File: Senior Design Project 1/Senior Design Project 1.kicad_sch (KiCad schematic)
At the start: 30 parts, among them U1 74LS05, U2 74HC273, U3 LM393NG, U6 LM555xN, U9 74HC273

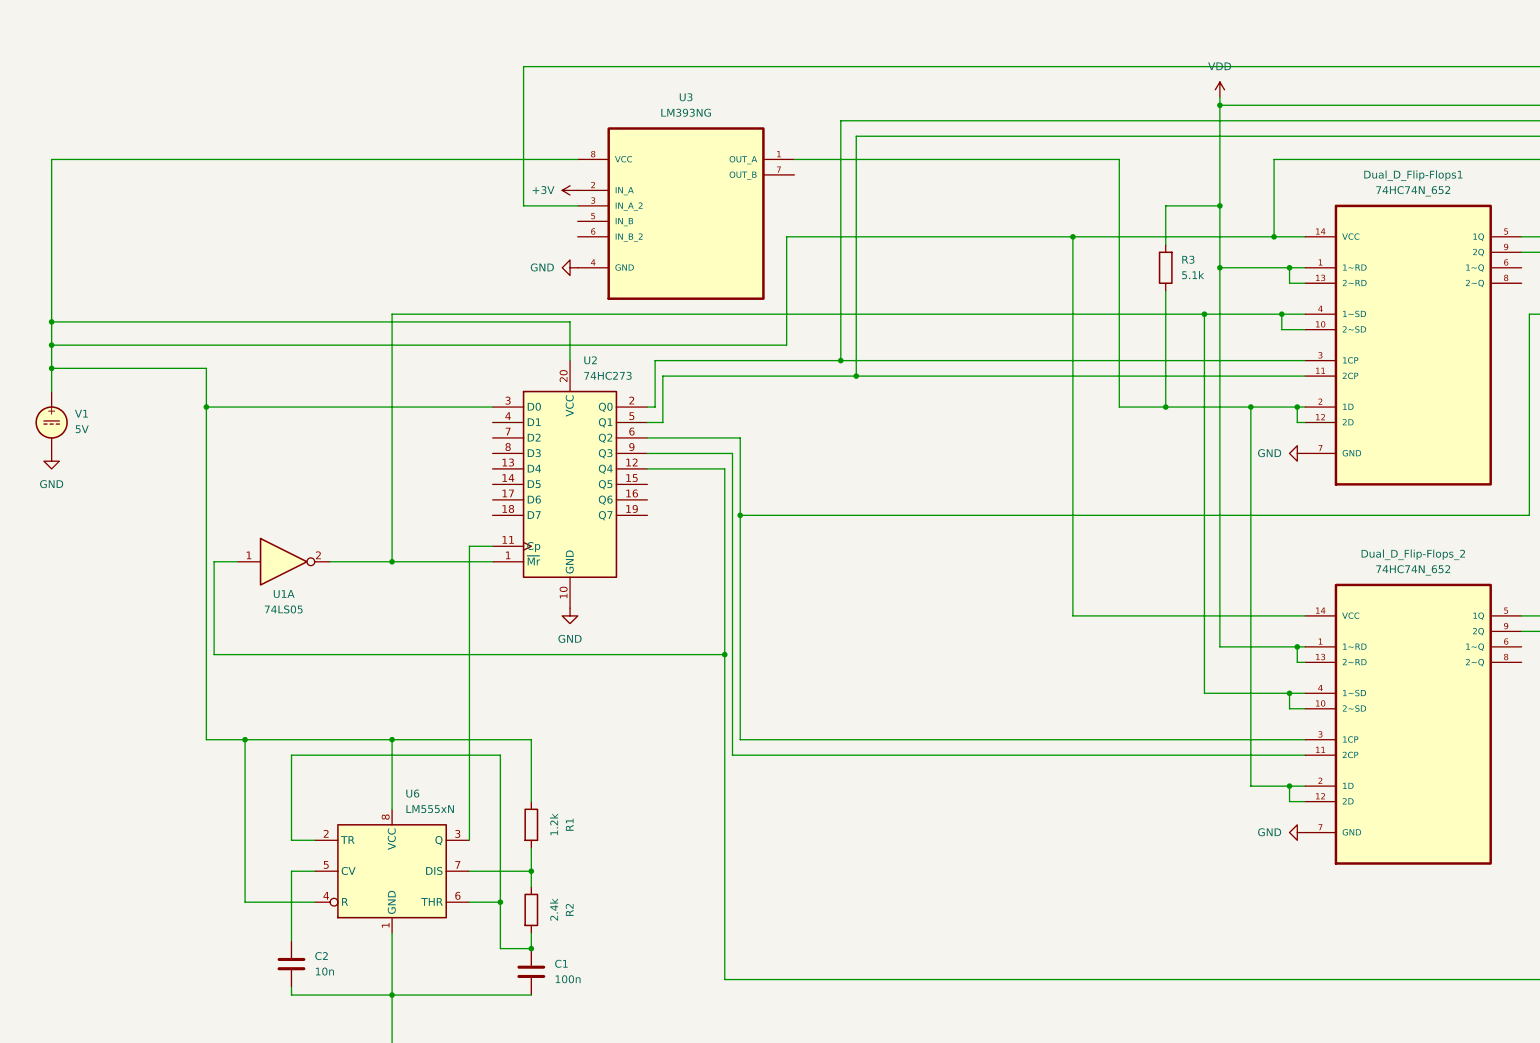
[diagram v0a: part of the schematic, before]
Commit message: Footprint fixes and updated PCB design
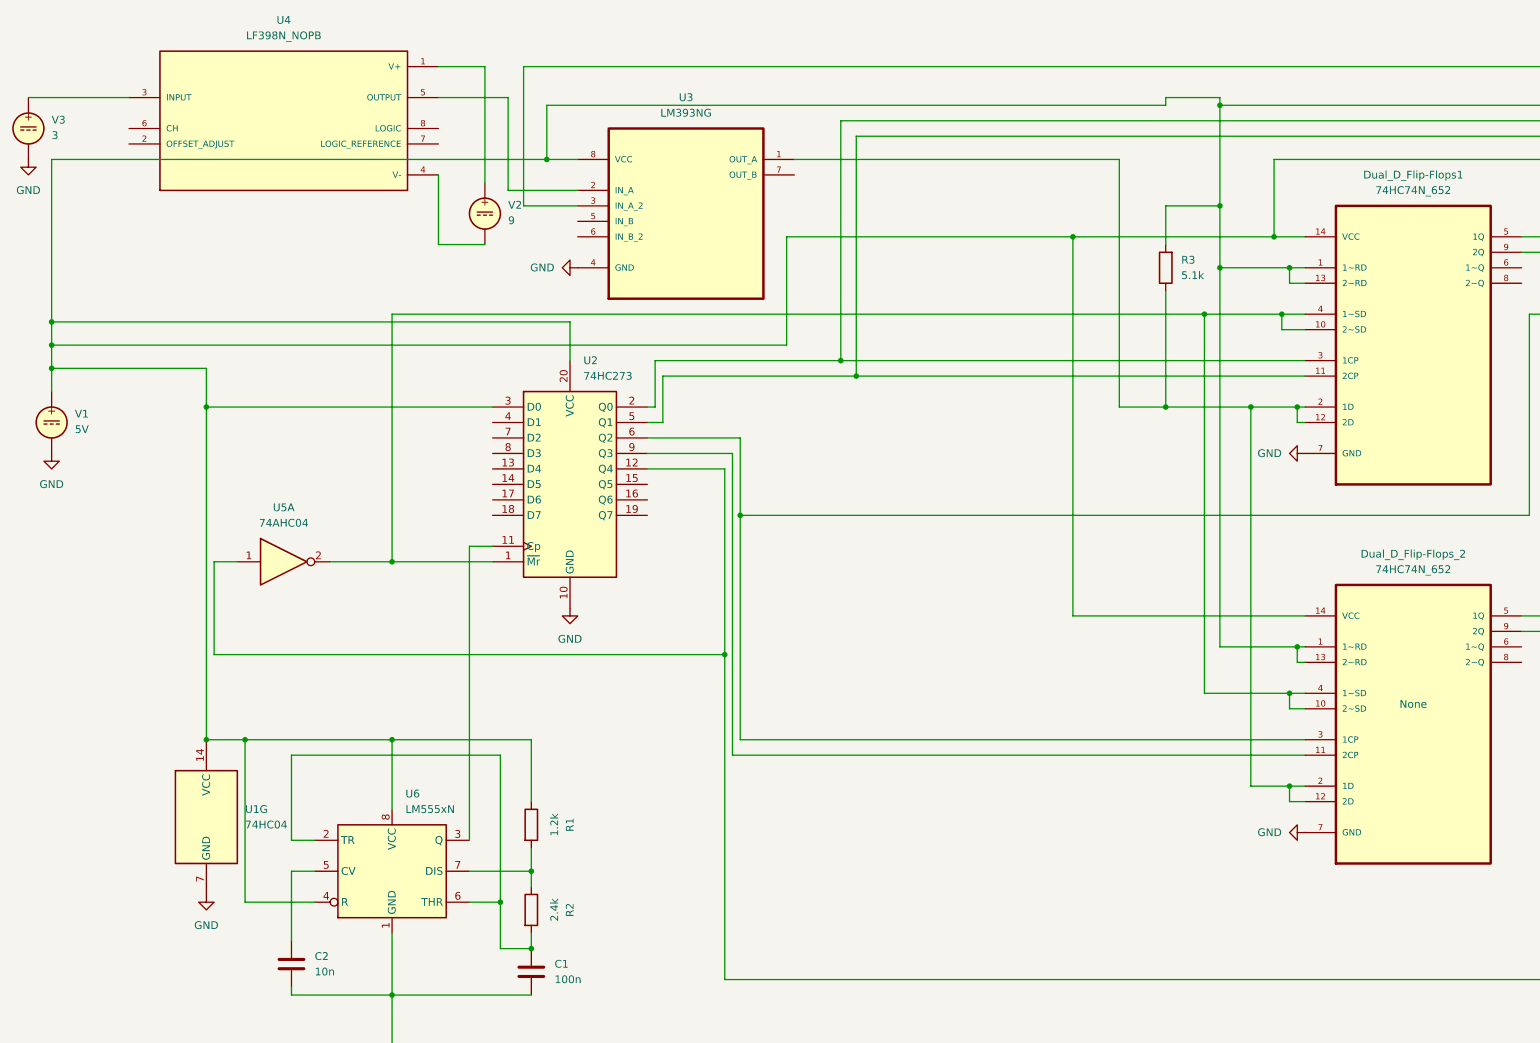
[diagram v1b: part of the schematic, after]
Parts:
- removed U1: 74LS05, RF_Mini-Circuits:Mini-Circuits_BK377, symbol 74xx:74LS05
- added U1: 74HC04, symbol 74xx:74HC04
- added U4: LF398N_NOPB, LF398N:DIP794W45P254L959H508Q8, symbol LF398N_NOPB:LF398N_NOPB
- added U5: 74AHC04, 74HC04N:DIP254P762X420-14, symbol 74xx:74AHC04
- added V2: 9, TerminalBlock_4Ucon:TerminalBlock_4Ucon_1x02_P3.50mm_Vertical, symbol Simulation_SPICE:VDC
- added V3: 3, TerminalBlock_4Ucon:TerminalBlock_4Ucon_1x02_P3.50mm_Vertical, symbol Simulation_SPICE:VDC
- Dual_D_Flip-Flops1, Dual_D_Flip-Flops_2: footprint 74HC74N_652:DIP254P762X420-14 -> 74HC74N Library:DIP254P762X420-14
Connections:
- net VDD is gone; now on an unnamed net: AND_Gates1.1 (1A), Dual_D_Flip-Flops1.1 (1~RD), Dual_D_Flip-Flops1.13 (2~RD), Dual_D_Flip-Flops_2.1 (1~RD), Dual_D_Flip-Flops_2.13 (2~RD), R3.2
- net GND: now also U1.7 (GND), V3.2
- net at Dual_D_Flip-Flops1.10 (2~SD), Dual_D_Flip-Flops1.4 (1~SD), Dual_D_Flip-Flops_2.10 (2~SD)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: now also U5.2
- net at AND_Gates1.14 (VCC), Dual_D_Flip-Flops1.14 (VCC), Dual_D_Flip-Flops_2.14 (VCC)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: now also U1.14 (VCC)
- net at U2.12 (Q4), U9.11 (Cp): now also U5.1
- net +3V: no longer names the net of U3.2 (IN_A)
- net +3V: now also U4.5 (OUTPUT)
- new net: U4.3 (INPUT), V3.1
- new net: U4.1 (V+), V2.1
- new net: U4.4 (V-), V2.2
